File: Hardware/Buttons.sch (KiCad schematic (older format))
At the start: 14 parts, among them J5 Buttons, SW1 Button_Plus, SW2 Button_Minus, SW3 Button_Settings

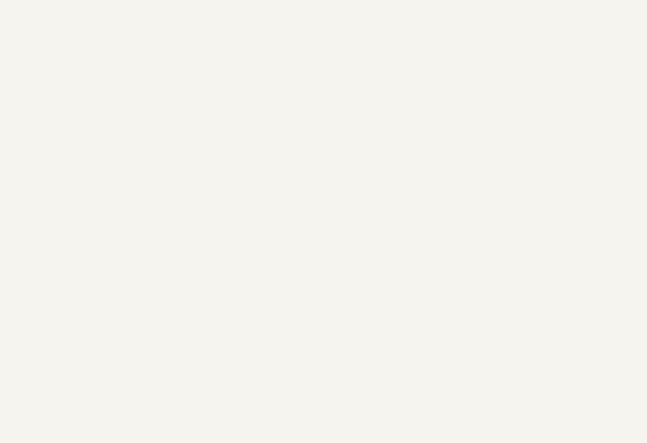
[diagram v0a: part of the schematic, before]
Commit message: [Hardware] Added alarm and backlight buttons parts to both schematic and PCB.
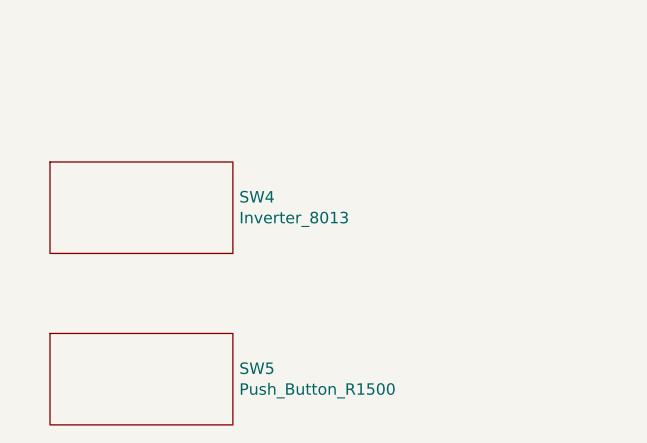
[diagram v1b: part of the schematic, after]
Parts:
- added SW4: Inverter_8013, Empty_Footprint:Empty_Footprint, symbol Switches:Inverter_8013
- added SW5: Push_Button_R1500, Empty_Footprint:Empty_Footprint, symbol Switches:Push_Button_R1500
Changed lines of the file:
@@
 Text HLabel 4900 4350 0    50   Output ~ 0
 BUTTON_SETTINGS
+$Comp
+L Switches:Inverter_8013 SW4
+U 1 1 5E7FA0CA
+P 1850 5100
+F 0 "SW4" H 2328 5146 50  0000 L CNN
+F 1 "Inverter_8013" H 2328 5055 50  0000 L CNN
+F 2 "Empty_Footprint:Empty_Footprint" H 1850 5100 50  0001 C CNN
+F 3 "https://www.gotronic.fr/art-inverseur-unipolaire-8013-4172.htm" H 1850 5100 50  0001 C CNN
+	1    1850 5100
+	1    0    0    -1
+$EndComp
+$Comp
+L Switches:Push_Button_R1500 SW5
+U 1 1 5E7FA7B1
+P 1900 5850
+F 0 "SW5" H 2328 5896 50  0000 L CNN
+F 1 "Push_Button_R1500" H 2328 5805 50  0000 L CNN
+F 2 "Empty_Footprint:Empty_Footprint" H 1900 5850 50  0001 C CNN
+F 3 "https://www.gotronic.fr/art-bp-de-securite-r1500-4191.htm" H 1900 5850 50  0001 C CNN
+	1    1900 5850
+	1    0    0    -1
+$EndComp
 $EndSCHEMATC

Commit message: [Hardware] Replaced each supply part by a generic one to avoid creating a new symbol for every supply part.
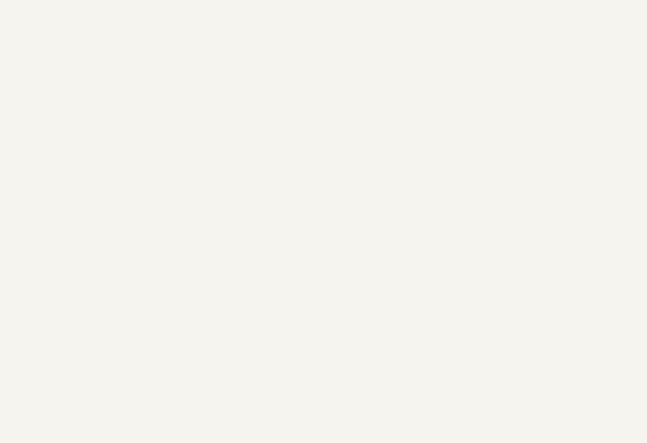
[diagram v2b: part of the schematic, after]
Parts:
- removed SW4: Inverter_8013, Empty_Footprint:Empty_Footprint, symbol Switches:Inverter_8013
- removed SW5: Push_Button_R1500, Empty_Footprint:Empty_Footprint, symbol Switches:Push_Button_R1500
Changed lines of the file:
@@
 $Descr A4 11693 8268
 encoding utf-8
-Sheet 4 4
+Sheet 4 5
 Title "All user interface buttons"
 Date ""
@@
 Text HLabel 4900 4350 0    50   Output ~ 0
 BUTTON_SETTINGS
-$Comp
-L Switches:Inverter_8013 SW4
-U 1 1 5E7FA0CA
-P 1850 5100
-F 0 "SW4" H 2328 5146 50  0000 L CNN
-F 1 "Inverter_8013" H 2328 5055 50  0000 L CNN
-F 2 "Empty_Footprint:Empty_Footprint" H 1850 5100 50  0001 C CNN
-F 3 "https://www.gotronic.fr/art-inverseur-unipolaire-8013-4172.htm" H 1850 5100 50  0001 C CNN
-	1    1850 5100
-	1    0    0    -1
-$EndComp
-$Comp
-L Switches:Push_Button_R1500 SW5
-U 1 1 5E7FA7B1
-P 1900 5850
-F 0 "SW5" H 2328 5896 50  0000 L CNN
-F 1 "Push_Button_R1500" H 2328 5805 50  0000 L CNN
-F 2 "Empty_Footprint:Empty_Footprint" H 1900 5850 50  0001 C CNN
-F 3 "https://www.gotronic.fr/art-bp-de-securite-r1500-4191.htm" H 1900 5850 50  0001 C CNN
-	1    1900 5850
-	1    0    0    -1
-$EndComp
 $EndSCHEMATC

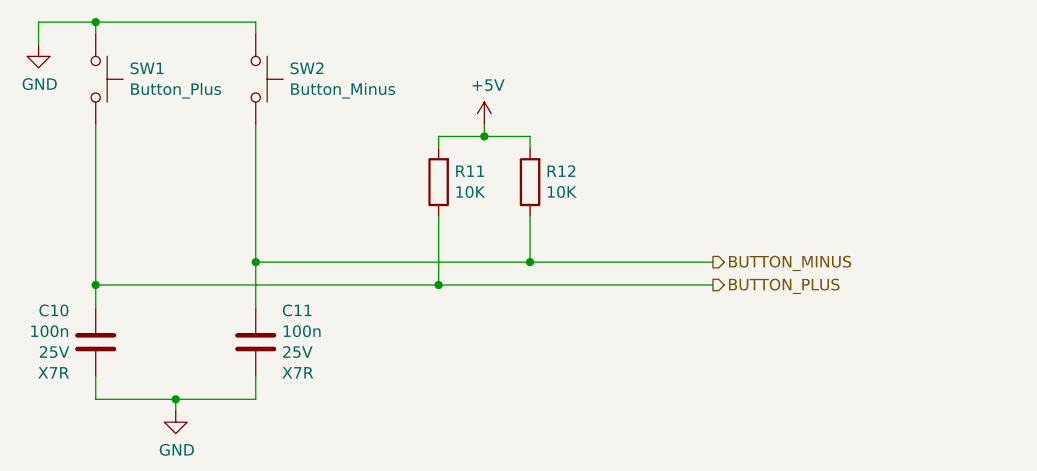
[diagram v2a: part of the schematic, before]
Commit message: [Hardware] Swapped 'plus' and 'minus' buttons in both schematic and PCB to match final buttons position.
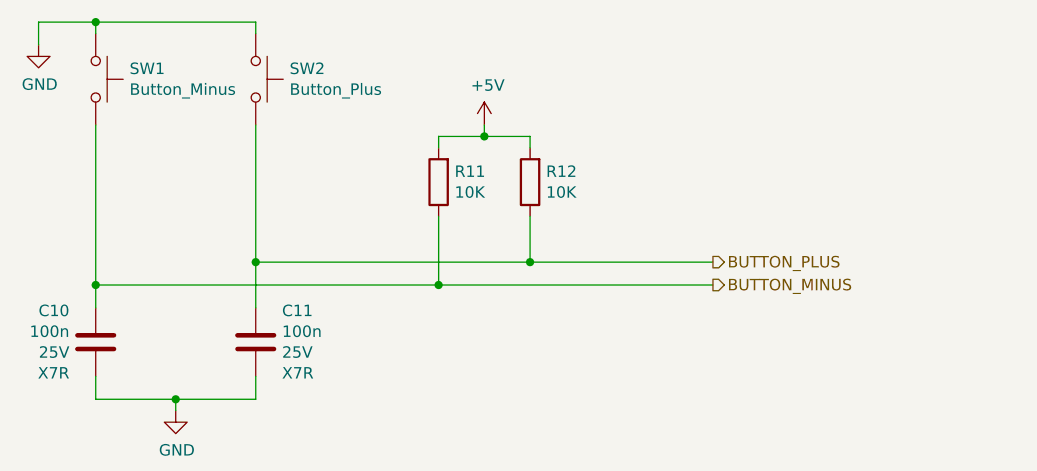
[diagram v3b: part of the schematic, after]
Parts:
- SW1: value Button_Plus -> Button_Minus
- SW2: value Button_Minus -> Button_Plus
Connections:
- net BUTTON_MINUS: now also C10.2, R11.1, SW1.2; no longer C11.2, R12.1, SW2.2
- net BUTTON_PLUS: now also C11.2, R12.1, SW2.2; no longer C10.2, R11.1, SW1.2
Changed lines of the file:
@@
 AR Path="/5E7CE147/5E7DE32A" Ref="SW2"  Part="1"
 F 0 "SW2" V 2354 1698 50  0000 L CNN
-F 1 "Button_Minus" V 2445 1698 50  0000 L CNN
+F 1 "Button_Plus" V 2445 1698 50  0000 L CNN
 F 2 "Button_Switch_THT:SW_Tactile_SKHH_Angled" H 2400 1750 50  0001 C CNN
 F 3 "~" H 2400 1750 50  0001 C CNN
@@
 AR Path="/5E7CE147/5E7DE330" Ref="SW1"  Part="1"
 F 0 "SW1" V 1654 1698 50  0000 L CNN
-F 1 "Button_Plus" V 1745 1698 50  0000 L CNN
+F 1 "Button_Minus" V 1745 1698 50  0000 L CNN
 F 2 "Button_Switch_THT:SW_Tactile_SKHH_Angled" H 1700 1750 50  0001 C CNN
 F 3 "~" H 1700 1750 50  0001 C CNN
@@
 	3600 2350 4400 2350
 Text HLabel 4400 2350 2    50   Output ~ 0
+BUTTON_PLUS
+Text HLabel 4400 2450 2    50   Output ~ 0
 BUTTON_MINUS
-Text HLabel 4400 2450 2    50   Output ~ 0
-BUTTON_PLUS
 $Comp
 L Switch:SW_Push SW?
